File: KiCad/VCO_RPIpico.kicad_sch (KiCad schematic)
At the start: 84 parts, among them J1 AudioJack3_Ground, J2 Power Jack, Q1 2N7002, SW1 LFO1/2, SW2 Select LFO WaveForm, SW3 Fire4, SW4 Fire3, SW5 Fire2, SW6 Fire1, SW7 Shift2/Save, SW8 Shift1 / Select Bank, U2 PT2399, U3 L7805

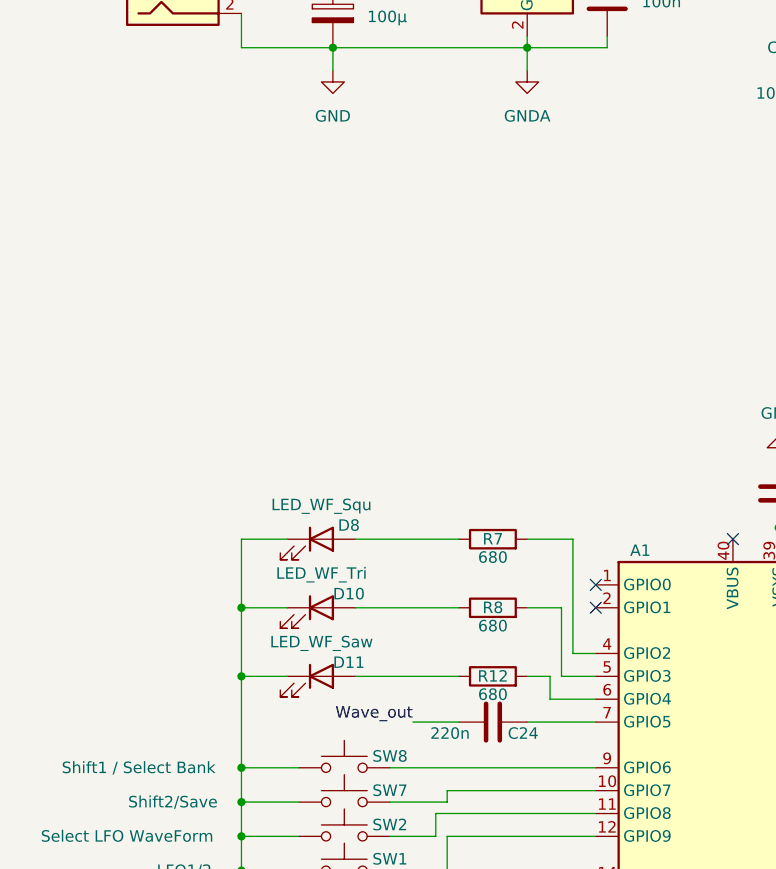
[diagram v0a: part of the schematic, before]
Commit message: Display SSD1306 added
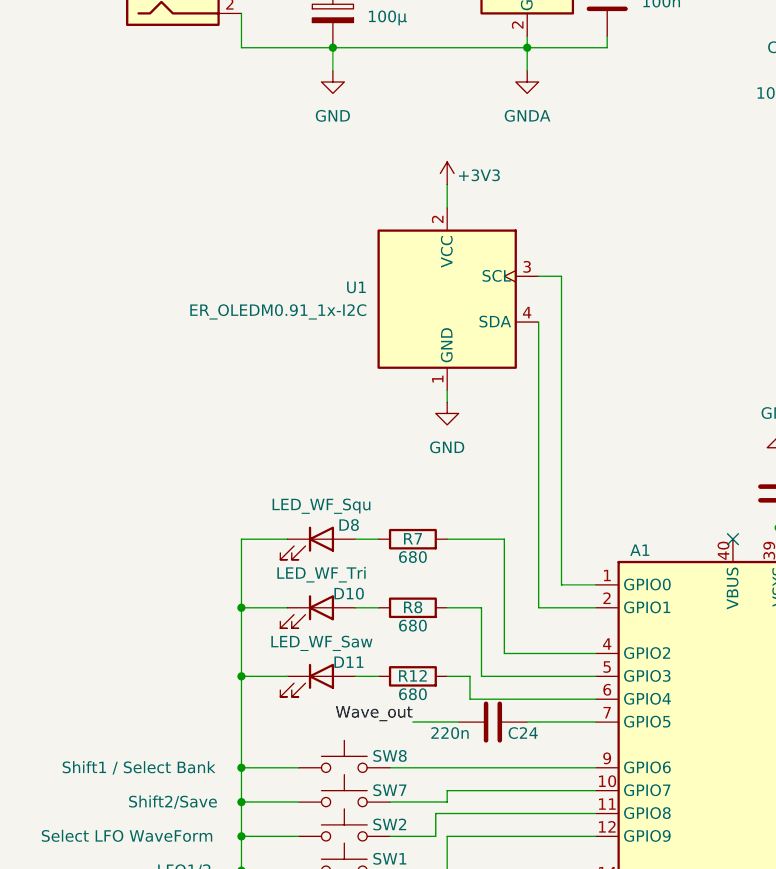
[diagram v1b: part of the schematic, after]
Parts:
- added U1: ER_OLEDM0.91_1x-I2C, Display:ER_OLEDM0.91_1x-I2C, symbol Display_Graphic:ER_OLEDM0.91_1x-I2C
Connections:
- net +3V3: now also U1.2 (VCC)
- net GND: now also U1.1 (GND)
- net at A1.1 (GPIO0): now also U1.3 (SCL)
- net at A1.2 (GPIO1): now also U1.4 (SDA)
- no-connect marks 10 -> 8
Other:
- moved on the sheet: R12, R7, R8

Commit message: change wiring on oled-display
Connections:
- net at U1.3 (SCL): now also A1.2 (GPIO1); no longer A1.1 (GPIO0)
- net at U1.4 (SDA): now also A1.1 (GPIO0); no longer A1.2 (GPIO1)
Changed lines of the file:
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@@
 	(wire
 		(pts
-			(xy 69.85 101.6) (xy 76.2 101.6)
+			(xy 73.66 101.6) (xy 76.2 101.6)
+		)
+		(stroke
+			(width 0)
+			(type default)
+		)
+	)
+	(wire
+		(pts
+			(xy 73.66 64.77) (xy 69.85 64.77)
 		)
 		(stroke
@@
 	(wire
 		(pts
+			(xy 72.39 69.85) (xy 69.85 69.85)
+		)
+		(stroke
+			(width 0)
+			(type default)
+		)
+	)
+	(wire
+		(pts
 			(xy 257.81 52.07) (xy 262.89 52.07)
 		)
@@
 	(wire
 		(pts
-			(xy 69.85 64.77) (xy 72.39 64.77)
-		)
-		(stroke
-			(width 0)
-			(type default)
-		)
-	)
-	(wire
-		(pts
 			(xy 53.34 127) (xy 58.42 127)
 		)
@@
 	(wire
 		(pts
-			(xy 72.39 64.77) (xy 72.39 99.06)
-		)
-		(stroke
-			(width 0)
-			(type default)
-		)
-	)
-	(wire
-		(pts
 			(xy 139.7 97.79) (xy 140.97 97.79)
 		)
@@
 	(wire
 		(pts
+			(xy 72.39 99.06) (xy 72.39 69.85)
+		)
+		(stroke
+			(width 0)
+			(type default)
+		)
+	)
+	(wire
+		(pts
 			(xy 36.83 170.18) (xy 39.37 170.18)
 		)
@@
 	(wire
 		(pts
+			(xy 73.66 64.77) (xy 73.66 101.6)
+		)
+		(stroke
+			(width 0)
+			(type default)
+		)
+	)
+	(wire
+		(pts
 			(xy 254 57.15) (xy 259.08 57.15)
 		)
@@
 		)
 		(stroke
-			(width 0)
-			(type default)
-		)
-	)
-	(wire
-		(pts
-			(xy 69.85 69.85) (xy 69.85 101.6)
-		)
-		(stroke

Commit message: datashaeets added
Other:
- note added: "SSD 1306"
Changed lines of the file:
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@@
+		)
+	)
+	(text "SSD 1306"
+		(exclude_from_sim no)
+		(at 45.974 71.628 0)
+		(effects
+			(font
+				(size 1.27 1.27)
+			)
 		)
 	)

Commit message: Display
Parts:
- C17, C18, C25: footprint Capacitor_Tantalum_SMD:CP_EIA-2012-12_Kemet-R_Pad1.30x1.05mm_HandSolder -> Capacitor_SMD:CP_Elec_4x5.7
- U1: footprint Display:ER_OLEDM0.91_1x-I2C -> Display:Adafruit_SSD1306
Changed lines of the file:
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@@
 			)
 		)
-		(property "Footprint" "Capacitor_Tantalum_SMD:CP_EIA-2012-12_Kemet-R_Pad1.30x1.05mm_HandSolder"
+		(property "Footprint" "Capacitor_SMD:CP_Elec_4x5.7"
 			(at 223.52 37.1348 0)
 			(hide yes)
@@
 		)
 		(property "Value" "GND"
-			(at 139.7 44.45 0)
+			(at 136.398 44.45 0)
 			(show_name no)
 			(do_not_autoplace no)
@@
 			)
 		)
-		(property "Footprint" "Display:ER_OLEDM0.91_1x-I2C"
+		(property "Footprint" "Display:Adafruit_SSD1306"
 			(at 41.656 80.01 0)
 			(hide yes)
@@
 			)
 		)
-		(property "Footprint" "Capacitor_Tantalum_SMD:CP_EIA-2012-12_Kemet-R_Pad1.30x1.05mm_HandSolder"
+		(property "Footprint" "Capacitor_SMD:CP_Elec_4x5.7"
 			(at 190.5 24.4348 0)
 			(hide yes)
@@
 			)
 		)
-		(property "Footprint" "Capacitor_Tantalum_SMD:CP_EIA-2012-12_Kemet-R_Pad1.30x1.05mm_HandSolder"
+		(property "Footprint" "Capacitor_SMD:CP_Elec_4x5.7"
 			(at 142.5448 27.94 0)
 			(hide yes)
